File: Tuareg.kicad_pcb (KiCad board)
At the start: 4 copper layers, 101.6 x 103.6 mm, 193 parts, among them CON1 ModICE_48, J1 SWD_boctok, P1 VNLD5090e, P2 FAN1100, P3 VNLD5090e, P4 FAN1100, P5 ISO7421D, Q1 BTS3028SDL, Q2 BTS3028SDL, Q3 ISL9V3040, Q4 BTS3028SDL, Q5 ISL9V3040, U1 NCV1117DT, U2 NCV1117ST, U3 MCP6004, U4 MCP6004, U5 MAX9926, U6 STM32F410RBTx, U7 24C64, Y1 lfxtal071673, Y2 cx5032ga

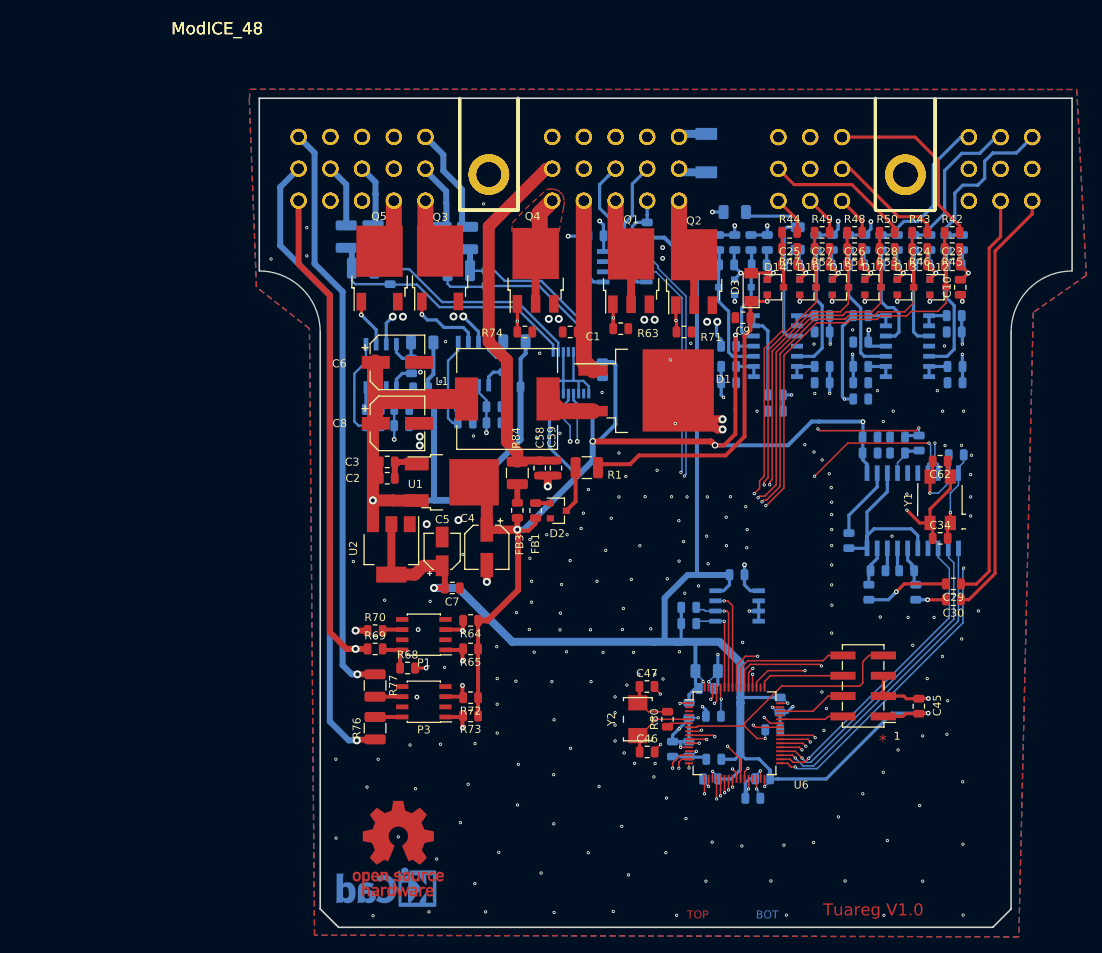
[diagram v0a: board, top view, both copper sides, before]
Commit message: changed to discrete crank vr sensor cirquitry
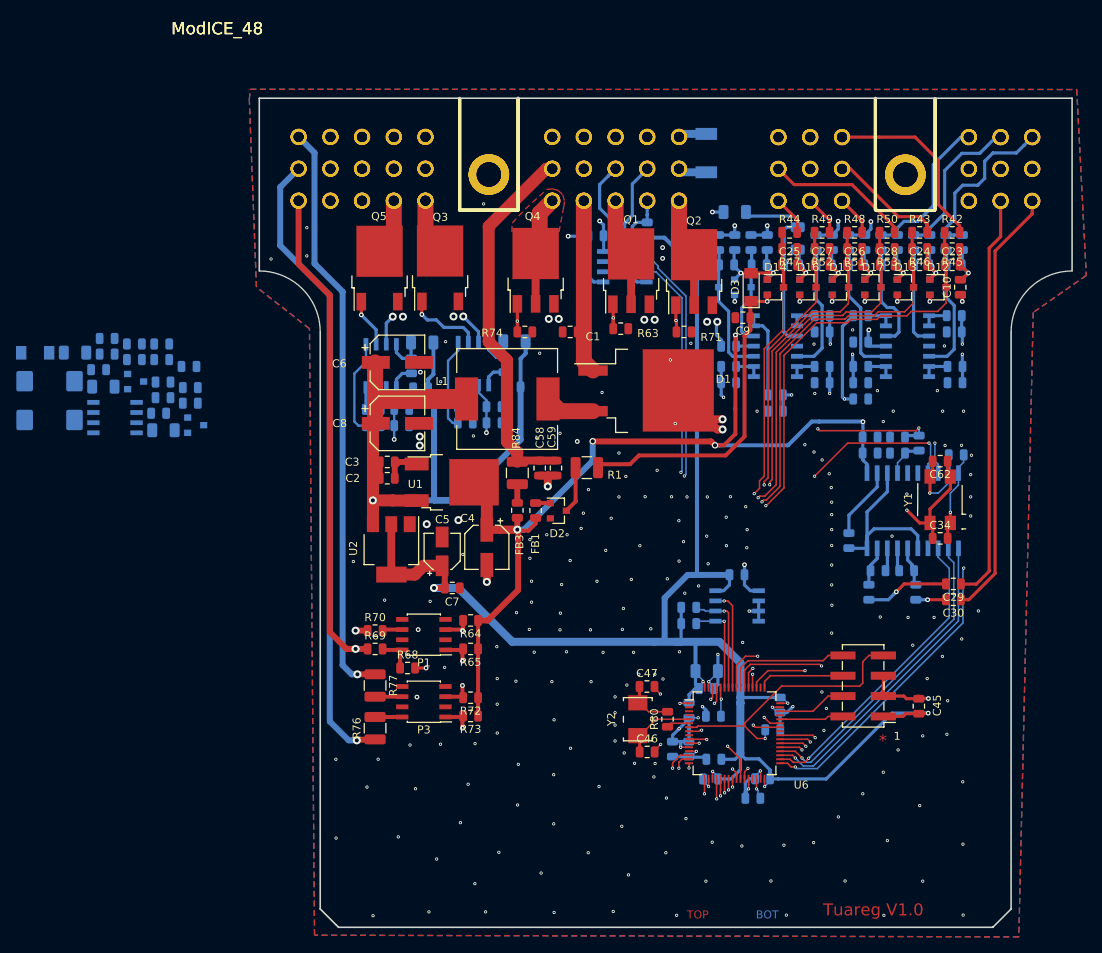
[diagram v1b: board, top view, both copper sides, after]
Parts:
- removed C580: 100nF, Capacitor_SMD:C_0805_2012Metric
- removed REF**: KiCad-Logo_5mm_Copper, Symbol:KiCad-Logo_5mm_Copper
- removed REF**: OSHW-Logo_11.4x12mm_Copper, Symbol:OSHW-Logo_11.4x12mm_Copper
- added C63: 100nF, Capacitor_SMD:C_0805_2012Metric, B.Cu at (65.1, 91.2)
- added C64: 5uF, Capacitor_SMD:C_1206_3216Metric, B.Cu at (65.7, 93.3)
- added C65: 10uF, Capacitor_Tantalum_SMD:CP_EIA-7343-31_Kemet-D, B.Cu at (51.5, 92.0)
- added C66: C, Capacitor_SMD:C_0805_2012Metric, B.Cu at (62.1, 84.5)
- added D20: BAT54S, Package_TO_SOT_SMD:SOT-23, B.Cu at (62.3, 87.2)
- added D21: BAT54A, Package_TO_SOT_SMD:SOT-23, B.Cu at (69.8, 92.7)
- added D22: D_Zener, Diode_SMD:D_MiniMELF, B.Cu at (49.7, 83.6)
- added R58: 16k, Resistor_SMD:R_0805_2012Metric, B.Cu at (65.5, 82.5)
- added R85: 62k, Resistor_SMD:R_0805_2012Metric, B.Cu at (68.9, 85.3)
- added R86: 330k, Resistor_SMD:R_0805_2012Metric, B.Cu at (58.7, 81.8)
- added R87: 5,1k, Resistor_SMD:R_0805_2012Metric, B.Cu at (65.7, 89.2)
- C21: value 100nF -> 10uF; footprint Capacitor_SMD:C_0805_2012Metric -> Capacitor_Tantalum_SMD:CP_EIA-7343-31_Kemet-D
- C22: value 100nF -> 1uF; footprint Capacitor_SMD:C_0805_2012Metric -> Capacitor_SMD:C_1206_3216Metric
- R34: footprint Resistor_SMD:R_1210_3225Metric -> Resistor_SMD:R_1206_3216Metric
- R35: value 10k -> 27k; footprint Resistor_SMD:R_1210_3225Metric -> Resistor_SMD:R_0805_2012Metric
- R36: value 10k -> 8,2k; footprint Resistor_SMD:R_1210_3225Metric -> Resistor_SMD:R_0805_2012Metric
- R37: value 10k -> 4,3k; footprint Resistor_SMD:R_1210_3225Metric -> Resistor_SMD:R_0805_2012Metric
- R38: value 5k -> 15k; footprint Resistor_SMD:R_1210_3225Metric -> Resistor_SMD:R_0805_2012Metric
- R39: value 5k -> 4,7k; footprint Resistor_SMD:R_1210_3225Metric -> Resistor_SMD:R_0805_2012Metric
- R40: value R -> 4,7k
- R41: value R -> 62k
- U5: value MAX9926 -> LM2903; footprint boctok_footprints:MAX99267 -> Package_SO:SOIC-8_3.9x4.9mm_P1.27mm
- moved U5 57.3 mm to (59.7, 91.7), turned to 0 degrees
- moved C21 56.2 mm to (51.5, 87.2), turned to 0 degrees
- moved R40 53.3 mm to (65.5, 84.5), turned to 0 degrees
- moved R34 51.1 mm to (54.7, 83.6), turned to 0 degrees
- moved R41 45.9 mm to (69.1, 88.0)
- moved R35 45.9 mm to (57.6, 85.7), turned to 0 degrees
- moved R38 39.5 mm to (65.7, 87.3)
- moved C22 38.4 mm to (58.2, 87.9), turned to 0 degrees
- moved R36 36.3 mm to (58.7, 83.8), turned to 0 degrees
- moved R39 30.1 mm to (62.1, 82.5), turned to 0 degrees
- moved R37 28.5 mm to (69.1, 89.9), turned to 0 degrees
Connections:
- C22 pad 1: Net-(C22-Pad1) -> +5V
- C22 pad 2: Net-(C22-Pad2) -> GND
- CON1 pad 34: /con_vrcrank- -> GND
- CON1 pad 36: /con_vrspare- -> Net-(CON1-Pad36)
- CON1 pad 37: /con_vrspare+ -> Net-(CON1-Pad37)
- R34 pad 2: Net-(C21-Pad1) -> GND
- R35 pad 1: /con_vrcrank- -> pwr_5v_clamp
- R35 pad 2: Net-(C21-Pad2) -> Net-(D20-Pad2)
- R36 pad 1: /con_vrspare- -> Net-(C21-Pad2)
- R36 pad 2: Net-(C22-Pad2) -> Net-(C21-Pad1)
- R37 pad 1: /con_vrspare+ -> Net-(C21-Pad1)
- R37 pad 2: Net-(C22-Pad1) -> GND
- R38 pad 1: Net-(C21-Pad2) -> Net-(C65-Pad1)
- R39 pad 1: Net-(C22-Pad2) -> Net-(C21-Pad1)
- R39 pad 2: Net-(C22-Pad1) -> Net-(D22-Pad1)
- R40 pad 1: +5V -> Net-(C66-Pad1)
- R40 pad 2: /crank -> Net-(D22-Pad1)
- R41 pad 2: /vr_spare -> Net-(C66-Pad1)
- U5 pad 1: GND -> /crank
- U5 pad 2: Net-(U5-Pad2) -> Net-(C66-Pad1)
- U5 pad 3: GND -> Net-(C66-Pad2)
- U5 pad 4: /crank -> GND
- U5 pad 5: /vr_spare -> GND
- U5 pad 7: Net-(U5-Pad7) -> GND
- U5 pad 8: GND -> +5V
- U6 pad 9: /vr_spare -> /cpu/PC1
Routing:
- net /vr_spare: track 70.3 -> 0.00 mm, vias 2 -> 0
- net Net-(C22-Pad1): track 33.6 -> 0.00 mm
- net Net-(C22-Pad2): track 31.4 -> 0.00 mm
- net +5V: track 186.8 -> 156.5 mm
- net Net-(C21-Pad2): track 26.2 -> 0.00 mm
- net Net-(C21-Pad1): track 22.9 -> 0.00 mm
- net GND: track 520.6 -> 503.6 mm
- net /con_vrcrank+: track 13.1 -> 0.00 mm
- net /con_vrspare+: track 7.93 -> 0.00 mm
- net /con_vrspare-: track 7.85 -> 0.00 mm
- net /con_vrcrank-: track 7.76 -> 0.00 mm
- net /crank: track 72.0 -> 66.0 mm

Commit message: fixed references to old kicad lib
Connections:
- C12 pad 1: GND -> Net-(C12-Pad1)
- C12 pad 2: /analog input/ch2_in -> Net-(C12-Pad2)
- R11 pad 1: /analog input/ch2_out -> Net-(R11-Pad1)
- R11 pad 2: /ach2 -> Net-(R11-Pad2)
- R15 pad 1: /ach2 -> Net-(R15-Pad1)
- R15 pad 2: GND -> Net-(R15-Pad2)
- R3 pad 1: /con_ach2 -> Net-(R3-Pad1)
- R3 pad 2: GND -> Net-(R3-Pad2)
- R7 pad 1: /con_ach2 -> Net-(R7-Pad1)
- R7 pad 2: /analog input/ch2_in -> Net-(R7-Pad2)
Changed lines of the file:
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@@
     (zones 0)
     (modules 201)
-    (nets 154)
+    (nets 164)
   )
   (page A4)
   (layers
-    (0 F.Cu mixed hide)
+    (0 F.Cu mixed)
     (1 VCC.Cu mixed)
     (2 GND.Cu mixed)
     (31 B.Cu mixed)
     (32 B.Adhes user)
-    (33 F.Adhes user hide)
+    (33 F.Adhes user)
     (34 B.Paste user)
-    (35 F.Paste user hide)
+    (35 F.Paste user)
     (36 B.SilkS user)
-    (37 F.SilkS user hide)
+    (37 F.SilkS user)
     (38 B.Mask user)
-    (39 F.Mask user hide)
-    (40 Dwgs.User user hide)
-    (41 Cmts.User user hide)
+    (39 F.Mask user)
+    (40 Dwgs.User user)
+    (41 Cmts.User user)
     (42 Eco1.User user)
     (43 Eco2.User user)
@@
     (45 Margin user)
     (46 B.CrtYd user)
-    (47 F.CrtYd user hide)
+    (47 F.CrtYd user)
     (48 B.Fab user)
-    (49 F.Fab user hide)
+    (49 F.Fab user)
   )
   (setup
@@
   (net 152 "Net-(D20-Pad2)")
   (net 153 "Net-(D22-Pad1)")
+  (net 154 "Net-(R11-Pad2)")
+  (net 155 "Net-(R11-Pad1)")
+  (net 156 "Net-(R15-Pad2)")
+  (net 157 "Net-(R15-Pad1)")
+  (net 158 "Net-(R7-Pad2)")
+  (net 159 "Net-(R7-Pad1)")
+  (net 160 "Net-(R3-Pad2)")
+  (net 161 "Net-(R3-Pad1)")
+  (net 162 "Net-(C12-Pad2)")
+  (net 163 "Net-(C12-Pad1)")
   (net_class Default "This is the default net class."
     (clearance 0.2)
@@
     (add_net /cpu/pwr_vdda)
     (add_net GND)
+    (add_net "Net-(C12-Pad1)")
+    (add_net "Net-(C12-Pad2)")
     (add_net "Net-(C29-Pad2)")
     (add_net "Net-(C30-Pad2)")
@@
     (add_net "Net-(P4-Pad5)")
     (add_net "Net-(P4-Pad6)")
+    (add_net "Net-(R11-Pad1)")
+    (add_net "Net-(R11-Pad2)")
+    (add_net "Net-(R15-Pad1)")
+    (add_net "Net-(R15-Pad2)")
+    (add_net "Net-(R3-Pad1)")
+    (add_net "Net-(R3-Pad2)")
+    (add_net "Net-(R7-Pad1)")
+    (add_net "Net-(R7-Pad2)")
     (add_net pwr_5v_clamp)
   )
@@
     (fp_line (start -1 -0.6) (end -1 0.6) (layer B.Fab) (width 0.1))
     (pad 2 smd roundrect (at 0.9375 0 180) (size 0.975 1.4) (layers B.Cu B.Paste B.Mask) (roundrect_rratio 0.25)
-      (net 137 "/analog input/ch2_in"))
+      (net 162 "Net-(C12-Pad2)"))
     (pad 1 smd roundrect (at -0.9375 0 180) (size 0.975 1.4) (layers B.Cu B.Paste B.Mask) (roundrect_rratio 0.25)
-      (net 1 GND))
+      (net 163 "Net-(C12-Pad1)"))
     (model ${KISYS3DMOD}/Capacitor_SMD.3dshapes/C_0805_2012Metric.wrl
       (at (xyz 0 0 0))
@@
     (fp_line (start -1 -0.6) (end -1 0.6) (layer B.Fab) (width 0.1))
     (pad 2 smd roundrect (at 0.9375 0 270) (size 0.975 1.4) (layers B.Cu B.Paste B.Mask) (roundrect_rratio 0.25)
-      (net 1 GND))
+      (net 160 "Net-(R3-Pad2)"))
     (pad 1 smd roundrect (at -0.9375 0 270) (size 0.975 1.4) (layers B.Cu B.Paste B.Mask) (roundrect_rratio 0.25)
-      (net 123 /con_ach2))
+      (net 161 "Net-(R3-Pad1)"))
     (model ${KISYS3DMOD}/Resistor_SMD.3dshapes/R_0805_2012Metric.wrl
       (at (xyz 0 0 0))
@@
     (fp_line (start -1 -0.6) (end -1 0.6) (layer B.Fab) (width 0.1))
     (pad 2 smd roundrect (at 0.9375 0 270) (size 0.975 1.4) (layers B.Cu B.Paste B.Mask) (roundrect_rratio 0.25)
-      (net 137 "/analog input/ch2_in"))
+      (net 158 "Net-(R7-Pad2)"))
     (pad 1 smd roundrect (at -0.9375 0 270) (size 0.975 1.4) (layers B.Cu B.Paste B.Mask) (roundrect_rratio 0.25)
-      (net 123 /con_ach2))
+      (net 159 "Net-(R7-Pad1)"))
     (model ${KISYS3DMOD}/Resistor_SMD.3dshapes/R_0805_2012Metric.wrl
       (at (xyz 0 0 0))
@@
     (fp_line (start -1 -0.6) (end -1 0.6) (layer B.Fab) (width 0.1))
     (pad 2 smd roundrect (at 0.9375 0 180) (size 0.975 1.4) (layers B.Cu B.Paste B.Mask) (roundrect_rratio 0.25)
-      (net 144 /ach2))
+      (net 154 "Net-(R11-Pad2)"))
     (pad 1 smd roundrect (at -0.9375 0 180) (size 0.975 1.4) (layers B.Cu B.Paste B.Mask) (roundrect_rratio 0.25)
-      (net 136 "/analog input/ch2_out"))
+      (net 155 "Net-(R11-Pad1)"))
     (model ${KISYS3DMOD}/Resistor_SMD.3dshapes/R_0805_2012Metric.wrl
       (at (xyz 0 0 0))
@@
     (fp_line (start -1 -0.6) (end -1 0.6) (layer B.Fab) (width 0.1))
     (pad 2 smd roundrect (at 0.9375 0) (size 0.975 1.4) (layers B.Cu B.Paste B.Mask) (roundrect_rratio 0.25)
-      (net 1 GND))
+      (net 156 "Net-(R15-Pad2)"))
     (pad 1 smd roundrect (at -0.9375 0) (size 0.975 1.4) (layers B.Cu B.Paste B.Mask) (roundrect_rratio 0.25)
-      (net 144 /ach2))
+      (net 157 "Net-(R15-Pad1)"))
     (model ${KISYS3DMOD}/Resistor_SMD.3dshapes/R_0805_2012Metric.wrl
       (at (xyz 0 0 0))

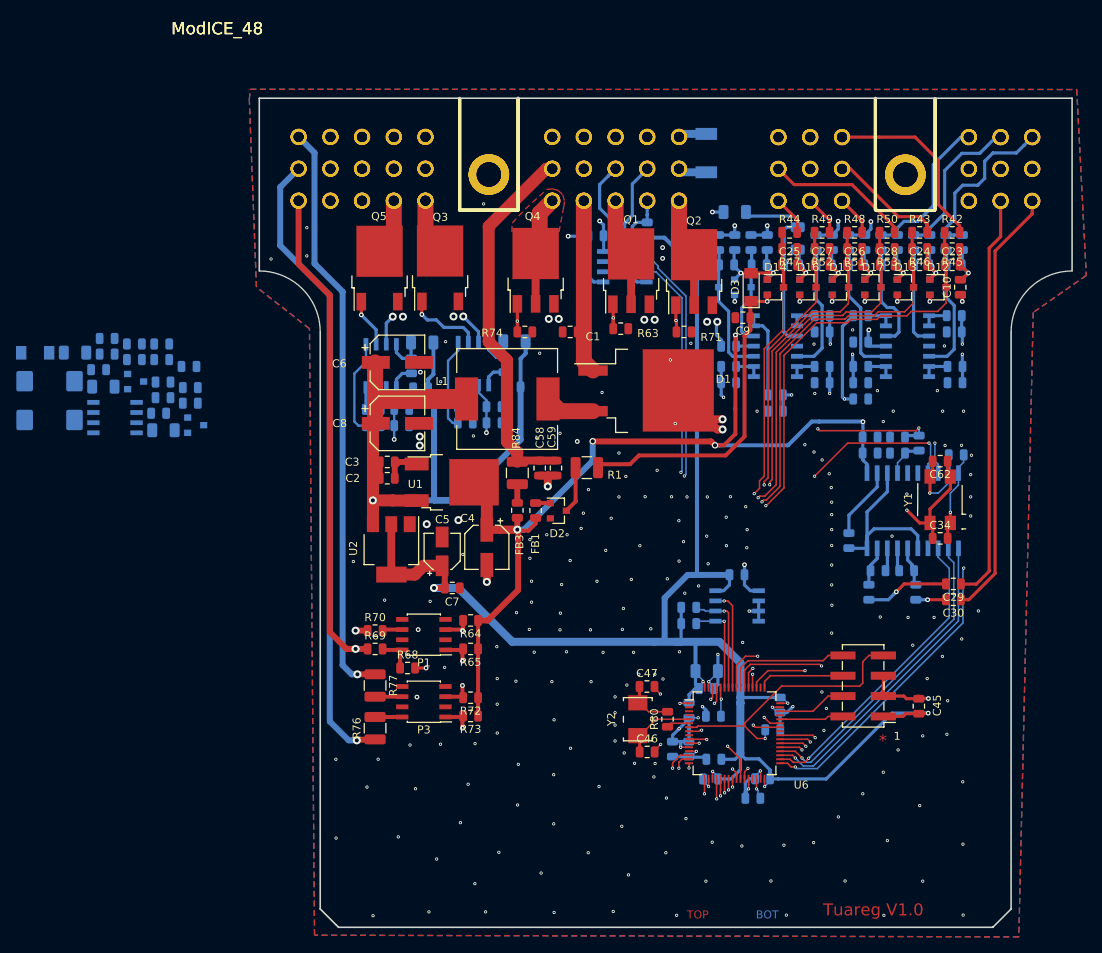
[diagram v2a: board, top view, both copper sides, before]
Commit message: migration to kicad 5.1.2
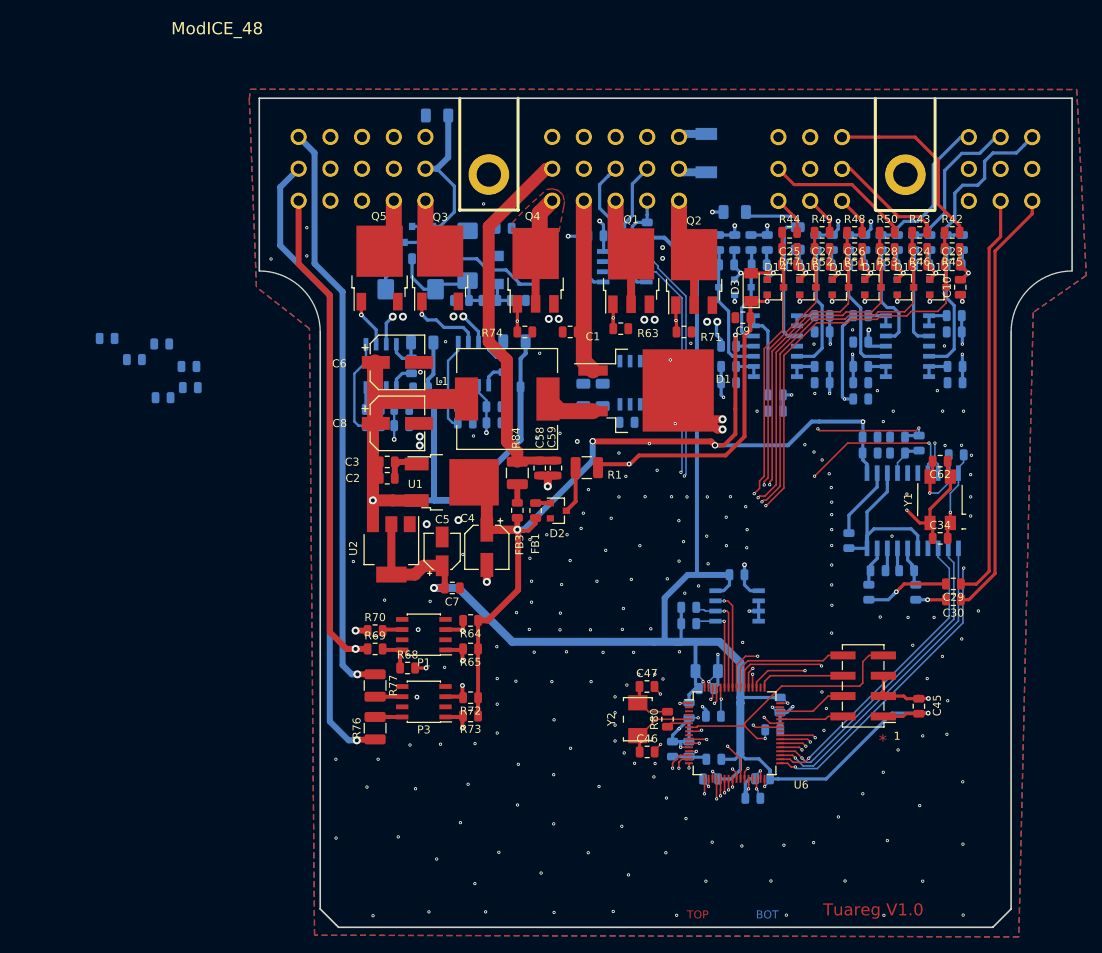
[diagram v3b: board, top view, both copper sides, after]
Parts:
- removed the CON1 at (77.7, 51.8)
- moved U5 65.2 mm to (124.7, 87.4), turned to 270 degrees
- moved C22 62.4 mm to (120.7, 88.9), turned to 90 degrees
- moved D22 58.6 mm to (107.4, 73.3), turned to 90 degrees
- moved C63 58.6 mm to (123.7, 92.3)
- moved C21 54.6 mm to (103.8, 71.5), turned to 90 degrees
- moved R34 54.1 mm to (99.9, 54.0), turned to 180 degrees
- moved C64 52.7 mm to (118.2, 88.9), turned to 90 degrees
- moved R36 52.1 mm to (108.3, 68.1)
- moved C65 48.0 mm to (96.6, 75.7)
- moved R40 45.2 mm to (110.1, 77.1), turned to 180 degrees
- moved R39 44.8 mm to (106.6, 77.1)
- moved R35 44.0 mm to (99.4, 71.9), turned to 180 degrees
- moved D20 41.5 mm to (99.4, 68.8), turned to 90 degrees
- moved R37 36.2 mm to (103.0, 77.1), turned to 180 degrees
- moved D21 35.4 mm to (95.9, 68.8), turned to 270 degrees
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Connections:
- C12 pad 1: Net-(C12-Pad1) -> GND
- C12 pad 2: Net-(C12-Pad2) -> /analog input/ch2_in
- CON1 pad 34: GND -> /con_vrcrank+
- CON1 pad 44: /con_vrcrank+ -> GND
- R11 pad 1: Net-(R11-Pad1) -> /analog input/ch2_out
- R11 pad 2: Net-(R11-Pad2) -> /ach2
- R15 pad 1: Net-(R15-Pad1) -> /ach2
- R15 pad 2: Net-(R15-Pad2) -> GND
- R3 pad 1: Net-(R3-Pad1) -> /con_ach2
- R3 pad 2: Net-(R3-Pad2) -> GND
- R7 pad 1: Net-(R7-Pad1) -> /con_ach2
- R7 pad 2: Net-(R7-Pad2) -> /analog input/ch2_in
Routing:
- net /con_vrcrank+: track 0.00 -> 21.0 mm
- net Net-(C21-Pad1): track 0.00 -> 14.3 mm
- net pwr_5v_clamp: track 80.7 -> 93.9 mm, vias 8 -> 9
- net Net-(C65-Pad1): track 0.00 -> 9.13 mm
- net Net-(D20-Pad2): track 0.00 -> 4.66 mm
- net Net-(C21-Pad2): track 0.00 -> 3.98 mm
- net Net-(D22-Pad1): track 0.00 -> 3.69 mm
- net GND: vias 237 -> 236
- net +5V: vias 6 -> 7
